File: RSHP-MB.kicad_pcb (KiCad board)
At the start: 2 copper layers, 120 x 120 mm, 23 parts, among them J1 Conn_02x20_Odd_Even, J2 Conn_02x02_Odd_Even, J3 Conn_02x02_Odd_Even, J4 Conn_02x04_Odd_Even

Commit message: Changed mount holes to M4 diameter. Generated CAM files.
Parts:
- H12, H13, H14, H15: footprint MountingHole:MountingHole_5.3mm_M5_Pad -> MountingHole:MountingHole_4.3mm_M4_Pad
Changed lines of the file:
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@@
   (paper "A4")
   (title_block
-    (title "RSHP-CB-0010")
-    (date "2022-05-22")
+    (title "RSHP-MB-0010")
+    (date "2022-05-25")
     (rev "1.0")
     (company "(c) Andriy Golovnya http://redscorp.net")
@@
       (net 2 "HE_GND") (pinfunction "1") (pintype "input"))
   )
-  (footprint "MountingHole:MountingHole_5.3mm_M5_Pad" (layer "F.Cu")
+  (footprint "MountingHole:MountingHole_4.3mm_M4_Pad" (layer "F.Cu")
     (at 57.5 142.5)
-    (descr "Mounting Hole 5.3mm, M5")
-    (tags "mounting hole 5.3mm m5")
-    (property "Sheetfile" "RSHP-MB.kicad_sch")
-    (property "Sheetname" "")
-    (attr exclude_from_pos_files)
-    (fp_text reference "H14" (at 0 -6.3) (layer "F.SilkS") hide
-      (effects (font (size 1 1) (thickness 0.15)))
-    )
-    (fp_text value "MountingHole" (at 0 6.3) (layer "F.Fab")
-      (effects (font (size 1 1) (thickness 0.15)))
-    )
-    (fp_text user "${REFERENCE}" (at 0 0) (layer "F.Fab")
-      (effects (font (size 1 1) (thickness 0.15)))
-    )
-    (fp_circle (center 0 0) (end 5.3 0) (layer "Cmts.User") (width 0.15) (fill none))
-    (fp_circle (center 0 0) (end 5.55 0) (layer "F.CrtYd") (width 0.05) (fill none))
-    (pad "1" thru_hole circle (at 0 0) (size 10.6 10.6) (drill 5.3) (layers *.Cu *.Mask)
+    (descr "Mounting Hole 4.3mm, M4")
+    (tags "mounting hole 4.3mm m4")
+    (property "Sheetfile" "RSHP-MB.kicad_sch")
+    (property "Sheetname" "")
+    (attr exclude_from_pos_files)
+    (fp_text reference "H14" (at 0 -5.3) (layer "F.SilkS")
+      (effects (font (size 1 1) (thickness 0.15)))
+    )
+    (fp_text value "MountingHole" (at 0 5.3) (layer "F.Fab")
+      (effects (font (size 1 1) (thickness 0.15)))
+    )
+    (fp_text user "${REFERENCE}" (at 0 0) (layer "F.Fab")
+      (effects (font (size 1 1) (thickness 0.15)))
+    )
+    (fp_circle (center 0 0) (end 4.3 0) (layer "Cmts.User") (width 0.15) (fill none))
+    (fp_circle (center 0 0) (end 4.55 0) (layer "F.CrtYd") (width 0.05) (fill none))
+    (pad "1" thru_hole circle (at 0 0) (size 8.6 8.6) (drill 4.3) (layers *.Cu *.Mask)
       (net 3 "EARTH") (pinfunction "1") (pintype "input"))
   )
@@
       (net 2 "HE_GND") (pinfunction "1") (pintype "input"))
   )
-  (footprint "MountingHole:MountingHole_5.3mm_M5_Pad" (layer "F.Cu")
+  (footprint "MountingHole:MountingHole_4.3mm_M4_Pad" (layer "F.Cu")
     (at 57.5 37.5)
-    (descr "Mounting Hole 5.3mm, M5")
-    (tags "mounting hole 5.3mm m5")
-    (property "Sheetfile" "RSHP-MB.kicad_sch")
-    (property "Sheetname" "")
-    (attr exclude_from_pos_files)
-    (fp_text reference "H12" (at 0 -6.3) (layer "F.SilkS") hide
-      (effects (font (size 1 1) (thickness 0.15)))
-    )
-    (fp_text value "MountingHole" (at 0 6.3) (layer "F.Fab")
-      (effects (font (size 1 1) (thickness 0.15)))
-    )
-    (fp_text user "${REFERENCE}" (at 0 0) (layer "F.Fab")
-      (effects (font (size 1 1) (thickness 0.15)))
-    )
-    (fp_circle (center 0 0) (end 5.3 0) (layer "Cmts.User") (width 0.15) (fill none))
-    (fp_circle (center 0 0) (end 5.55 0) (layer "F.CrtYd") (width 0.05) (fill none))
-    (pad "1" thru_hole circle (at 0 0) (size 10.6 10.6) (drill 5.3) (layers *.Cu *.Mask)
+    (descr "Mounting Hole 4.3mm, M4")
+    (tags "mounting hole 4.3mm m4")
+    (property "Sheetfile" "RSHP-MB.kicad_sch")
+    (property "Sheetname" "")
+    (attr exclude_from_pos_files)
+    (fp_text reference "H12" (at 0 -5.3) (layer "F.SilkS")
+      (effects (font (size 1 1) (thickness 0.15)))
+    )
+    (fp_text value "MountingHole" (at 0 5.3) (layer "F.Fab")
+      (effects (font (size 1 1) (thickness 0.15)))
+    )
+    (fp_text user "${REFERENCE}" (at 0 0) (layer "F.Fab")
+      (effects (font (size 1 1) (thickness 0.15)))
+    )
+    (fp_circle (center 0 0) (end 4.3 0) (layer "Cmts.User") (width 0.15) (fill none))
+    (fp_circle (center 0 0) (end 4.55 0) (layer "F.CrtYd") (width 0.05) (fill none))
+    (pad "1" thru_hole circle (at 0 0) (size 8.6 8.6) (drill 4.3) (layers *.Cu *.Mask)
       (net 3 "EARTH") (pinfunction "1") (pintype "input"))
   )
-  (footprint "MountingHole:MountingHole_5.3mm_M5_Pad" (layer "F.Cu")
+  (footprint "MountingHole:MountingHole_4.3mm_M4_Pad" (layer "F.Cu")
     (at 162.5 142.5)
-    (descr "Mounting Hole 5.3mm, M5")
-    (tags "mounting hole 5.3mm m5")
-    (property "Sheetfile" "RSHP-MB.kicad_sch")
-    (property "Sheetname" "")
-    (attr exclude_from_pos_files)
-    (fp_text reference "H15" (at 0 -6.3) (layer "F.SilkS") hide
-      (effects (font (size 1 1) (thickness 0.15)))
-    )
-    (fp_text value "MountingHole" (at 0 6.3) (layer "F.Fab")
-      (effects (font (size 1 1) (thickness 0.15)))
-    )
-    (fp_text user "${REFERENCE}" (at 0 0) (layer "F.Fab")
-      (effects (font (size 1 1) (thickness 0.15)))
-    )
-    (fp_circle (center 0 0) (end 5.3 0) (layer "Cmts.User") (width 0.15) (fill none))
-    (fp_circle (center 0 0) (end 5.55 0) (layer "F.CrtYd") (width 0.05) (fill none))
-    (pad "1" thru_hole circle (at 0 0) (size 10.6 10.6) (drill 5.3) (layers *.Cu *.Mask)
+    (descr "Mounting Hole 4.3mm, M4")
+    (tags "mounting hole 4.3mm m4")
+    (property "Sheetfile" "RSHP-MB.kicad_sch")
+    (property "Sheetname" "")
+    (attr exclude_from_pos_files)
+    (fp_text reference "H15" (at 0 -5.3) (layer "F.SilkS")
+      (effects (font (size 1 1) (thickness 0.15)))
+    )
+    (fp_text value "MountingHole" (at 0 5.3) (layer "F.Fab")
+      (effects (font (size 1 1) (thickness 0.15)))
+    )
+    (fp_text user "${REFERENCE}" (at 0 0) (layer "F.Fab")
+      (effects (font (size 1 1) (thickness 0.15)))
+    )
+    (fp_circle (center 0 0) (end 4.3 0) (layer "Cmts.User") (width 0.15) (fill none))
+    (fp_circle (center 0 0) (end 4.55 0) (layer "F.CrtYd") (width 0.05) (fill none))
+    (pad "1" thru_hole circle (at 0 0) (size 8.6 8.6) (drill 4.3) (layers *.Cu *.Mask)
       (net 3 "EARTH") (pinfunction "1") (pintype "input"))
   )
@@
       (net 2 "HE_GND") (pinfunction "1") (pintype "input"))
   )
-  (footprint "MountingHole:MountingHole_5.3mm_M5_Pad" (layer "F.Cu")
+  (footprint "MountingHole:MountingHole_4.3mm_M4_Pad" (layer "F.Cu")
     (at 162.5 37.5)
-    (descr "Mounting Hole 5.3mm, M5")
-    (tags "mounting hole 5.3mm m5")
-    (property "Sheetfile" "RSHP-MB.kicad_sch")
-    (property "Sheetname" "")
-    (attr exclude_from_pos_files)
-    (fp_text reference "H13" (at 0 -6.3) (layer "F.SilkS") hide
-      (effects (font (size 1 1) (thickness 0.15)))
-    )
-    (fp_text value "MountingHole" (at 0 6.3) (layer "F.Fab")
-      (effects (font (size 1 1) (thickness 0.15)))
-    )
-    (fp_text user "${REFERENCE}" (at 0 0) (layer "F.Fab")
-      (effects (font (size 1 1) (thickness 0.15)))
-    )
-    (fp_circle (center 0 0) (end 5.3 0) (layer "Cmts.User") (width 0.15) (fill none))
-    (fp_circle (center 0 0) (end 5.55 0) (layer "F.CrtYd") (width 0.05) (fill none))
-    (pad "1" thru_hole circle (at 0 0) (size 10.6 10.6) (drill 5.3) (layers *.Cu *.Mask)
+    (descr "Mounting Hole 4.3mm, M4")
+    (tags "mounting hole 4.3mm m4")
+    (property "Sheetfile" "RSHP-MB.kicad_sch")
+    (property "Sheetname" "")
+    (attr exclude_from_pos_files)
+    (fp_text reference "H13" (at 0 -5.3) (layer "F.SilkS")
+      (effects (font (size 1 1) (thickness 0.15)))
+    )
+    (fp_text value "MountingHole" (at 0 5.3) (layer "F.Fab")
+      (effects (font (size 1 1) (thickness 0.15)))
+    )
+    (fp_text user "${REFERENCE}" (at 0 0) (layer "F.Fab")
+      (effects (font (size 1 1) (thickness 0.15)))
+    )
+    (fp_circle (center 0 0) (end 4.3 0) (layer "Cmts.User") (width 0.15) (fill none))
+    (fp_circle (center 0 0) (end 4.55 0) (layer "F.CrtYd") (width 0.05) (fill none))
+    (pad "1" thru_hole circle (at 0 0) (size 8.6 8.6) (drill 4.3) (layers *.Cu *.Mask)
       (net 3 "EARTH") (pinfunction "1") (pintype "input"))
   )

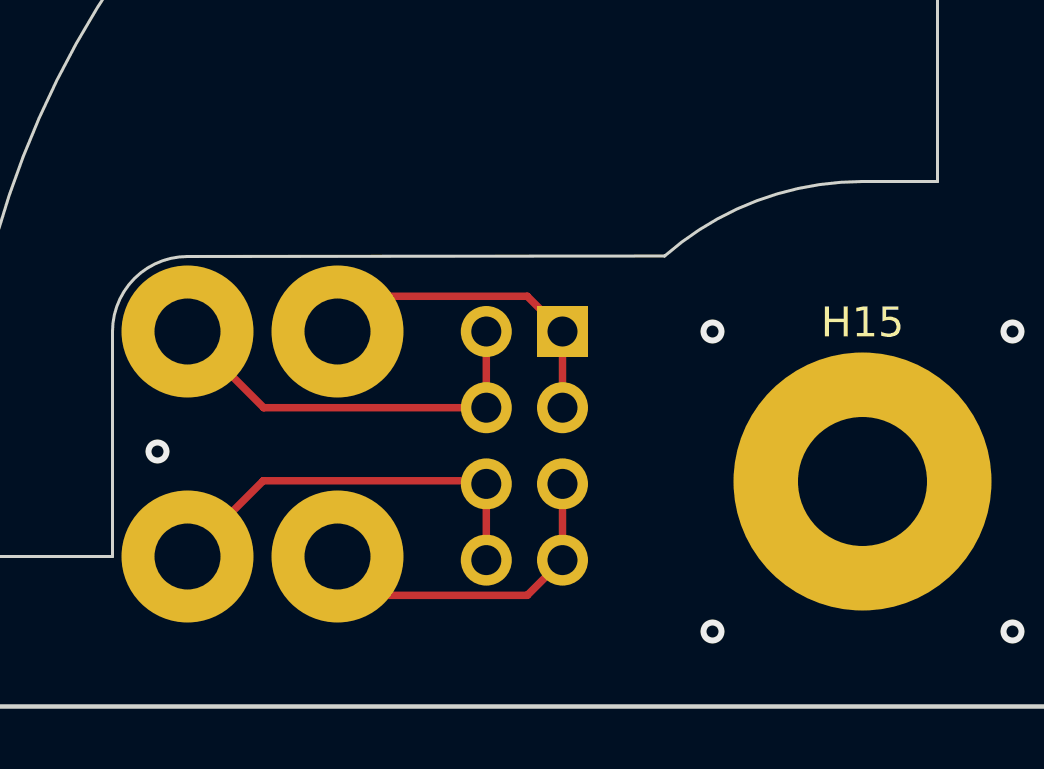
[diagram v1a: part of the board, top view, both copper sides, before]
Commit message: Made TR1 and TR2 wires thicker. Generated CAM files.
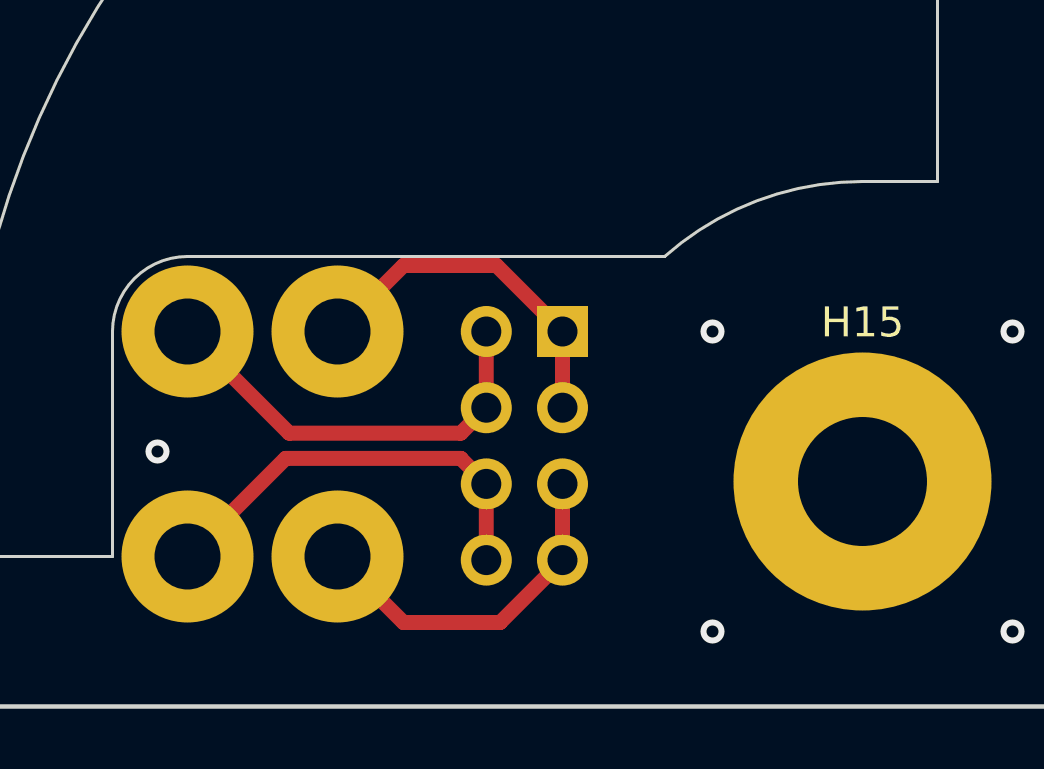
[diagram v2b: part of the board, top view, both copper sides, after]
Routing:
- net TR1_GND: track 11.6 -> 12.5 mm
- net TR2_GND: track 11.6 -> 12.4 mm
- net TR1_VCC: track 13.6 -> 14.3 mm
- net TR2_VCC: track 13.6 -> 14.2 mm
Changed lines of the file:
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@@
   (title_block
     (title "RSHP-MB-0010")
-    (date "2022-05-25")
+    (date "2022-05-29")
     (rev "1.0")
     (company "(c) Andriy Golovnya http://redscorp.net")
@@
   (gr_line (start 152.5 35) (end 132.5 35) (layer "Edge.Cuts") (width 0.1))
   (gr_arc (start 147.505592 63.484519) (mid 136.520843 52.503025) (end 132.5 37.5) (layer "Edge.Cuts") (width 0.1))
-  (gr_arc (start 155.905933 134.983519) (mid 158.976877 133.141462) (end 162.5 132.5) (layer "Edge.Cuts") (width 0.1))
+  (gr_arc (start 155.905933 135) (mid 158.973964 133.145977) (end 162.5 132.5) (layer "Edge.Cuts") (width 0.1))
   (gr_arc (start 60 47.5) (mid 58.535534 51.035534) (end 55 52.5) (layer "Edge.Cuts") (width 0.1))
   (gr_arc (start 132.5 142.5) (mid 141.286797 121.286797) (end 162.5 112.5) (layer "Edge.Cuts") (width 0.1))
@@
   (gr_line (start 162.5 132.5) (end 165 132.5) (layer "Edge.Cuts") (width 0.1))
   (gr_line (start 87.5 145) (end 87.5 142.5) (layer "Edge.Cuts") (width 0.1))
-  (gr_line (start 140 135) (end 155.905933 134.983519) (layer "Edge.Cuts") (width 0.1))
+  (gr_line (start 140 135) (end 155.905933 135) (layer "Edge.Cuts") (width 0.1))
   (gr_line (start 67.5 35) (end 87.5 35) (layer "Edge.Cuts") (width 0.1))
   (gr_arc (start 137.5 137.5) (mid 138.232233 135.732233) (end 140 135) (layer "Edge.Cuts") (width 0.1))
@@
   (via (at 52.5 147.5) (size 0.8) (drill 0.4) (layers "F.Cu" "B.Cu") (free) (net 3))
   (via (at 140 60) (size 0.8) (drill 0.4) (layers "F.Cu" "B.Cu") (free) (net 3))
-  (segment (start 149.96 140.04) (end 142.54 140.04) (width 0.25) (layer "F.Cu") (net 4))
-  (segment (start 149.96 140.04) (end 149.96 137.5) (width 0.25) (layer "F.Cu") (net 4))
-  (segment (start 142.54 140.04) (end 140 137.5) (width 0.25) (layer "F.Cu") (net 4))
-  (segment (start 151.325489 136.325489) (end 146.174511 136.325489) (width 0.25) (layer "F.Cu") (net 5))
-  (segment (start 152.5 140.04) (end 152.5 137.5) (width 0.25) (layer "F.Cu") (net 5))
-  (segment (start 152.5 137.5) (end 151.325489 136.325489) (width 0.25) (layer "F.Cu") (net 5))
-  (segment (start 146.174511 136.325489) (end 145 137.5) (width 0.25) (layer "F.Cu") (net 5))
+  (segment (start 149.96 140.04) (end 149.11 140.89) (width 0.5) (layer "F.Cu") (net 4))
+  (segment (start 149.11 140.89) (end 143.39 140.89) (width 0.5) (layer "F.Cu") (net 4))
+  (segment (start 149.96 140.04) (end 149.96 137.5) (width 0.5) (layer "F.Cu") (net 4))
+  (segment (start 143.39 140.89) (end 140 137.5) (width 0.5) (layer "F.Cu") (net 4))
   (segment (start 152.5 137.5) (end 153.135718 137.5) (width 0.25) (layer "F.Cu") (net 5))
-  (segment (start 149.96 145.12) (end 149.96 142.58) (width 0.25) (layer "F.Cu") (net 6))
-  (segment (start 149.855489 142.475489) (end 142.524511 142.475489) (width 0.25) (layer "F.Cu") (net 6))
-  (segment (start 142.524511 142.475489) (end 140 145) (width 0.25) (layer "F.Cu") (net 6))
-  (segment (start 149.96 142.58) (end 149.855489 142.475489) (width 0.25) (layer "F.Cu") (net 6))
-  (segment (start 146.294511 146.294511) (end 145 145) (width 0.25) (layer "F.Cu") (net 7))
+  (segment (start 147.199999 135.300001) (end 145 137.5) (width 0.5) (layer "F.Cu") (net 5))
+  (segment (start 150.300001 135.300001) (end 147.199999 135.300001) (width 0.5) (layer "F.Cu") (net 5))
+  (segment (start 152.5 137.5) (end 150.300001 135.300001) (width 0.5) (layer "F.Cu") (net 5))
+  (segment (start 152.5 140.04) (end 152.5 137.5) (width 0.5) (layer "F.Cu") (net 5))
+  (segment (start 149.11 141.73) (end 143.27 141.73) (width 0.5) (layer "F.Cu") (net 6))
+  (segment (start 149.96 145.12) (end 149.96 142.58) (width 0.5) (layer "F.Cu") (net 6))
+  (segment (start 143.27 141.73) (end 140 145) (width 0.5) (layer "F.Cu") (net 6))
+  (segment (start 149.96 142.58) (end 149.11 141.73) (width 0.5) (layer "F.Cu") (net 6))
+  (segment (start 152.5 145.12) (end 150.420001 147.199999) (width 0.5) (layer "F.Cu") (net 7))
+  (segment (start 147.199999 147.199999) (end 145 145) (width 0.5) (layer "F.Cu") (net 7))
   (segment (start 152.5 142.58) (end 153.055718 142.58) (width 0.25) (layer "F.Cu") (net 7))
-  (segment (start 151.325489 146.294511) (end 146.294511 146.294511) (width 0.25) (layer "F.Cu") (net 7))
-  (segment (start 152.5 145.12) (end 151.325489 146.294511) (width 0.25) (layer "F.Cu") (net 7))
-  (segment (start 152.5 145.12) (end 152.5 142.58) (width 0.25) (layer "F.Cu") (net 7))
+  (segment (start 152.5 145.12) (end 152.5 142.58) (width 0.5) (layer "F.Cu") (net 7))
+  (segment (start 150.420001 147.199999) (end 147.199999 147.199999) (width 0.5) (layer "F.Cu") (net 7))
   (zone (net 1) (net_name "HE_VCC") (layers F&B.Cu) (hatch edge 0.508)
     (priority 1)
